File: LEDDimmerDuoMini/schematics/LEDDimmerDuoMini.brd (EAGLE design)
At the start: 82.2 x 22.9 mm, 13 parts, among them IC1 7805T, T1 2N3904, T2 2N3904

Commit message: Update before LED flaate testen
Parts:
- added R3, R4: (no value), eagle-ltspice:R0805
- moved Q2 5.68 mm to (33.0, 6.35), turned to 90 degrees
- moved C2 5.08 mm to (69.8, 14.0)
- moved C3 5.08 mm to (69.8, 9.53)
- moved IC1 5.08 mm to (64.8, 11.4)
- moved MINI_TWI 5.08 mm to (80.0, 12.1)
- moved TWI_PORT 5.08 mm to (84.5, 12.1)
- moved T2 4.62 mm to (40.6, 3.81), turned to 270 degrees
- moved R2 2.84 mm to (16.5, 6.35)
- moved JP1 2.54 mm to (59.7, 19.1)
- moved JP2 2.54 mm to (59.7, 3.81)
- moved Q1 2.54 mm to (33.0, 17.8), turned to 90 degrees
- moved T1 1.80 mm to (40.6, 15.2), turned to 270 degrees
- moved R1 1.80 mm to (16.5, 16.5)
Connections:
- new net N$7: Q2.G, R4.2, T2.3
- net PWM1: now also R3.1, R3.2
- net PWM2: now also R4.1; no longer Q2.G, T2.3
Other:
- board size 82.2 x 22.9 mm -> 87.3 x 22.9 mm

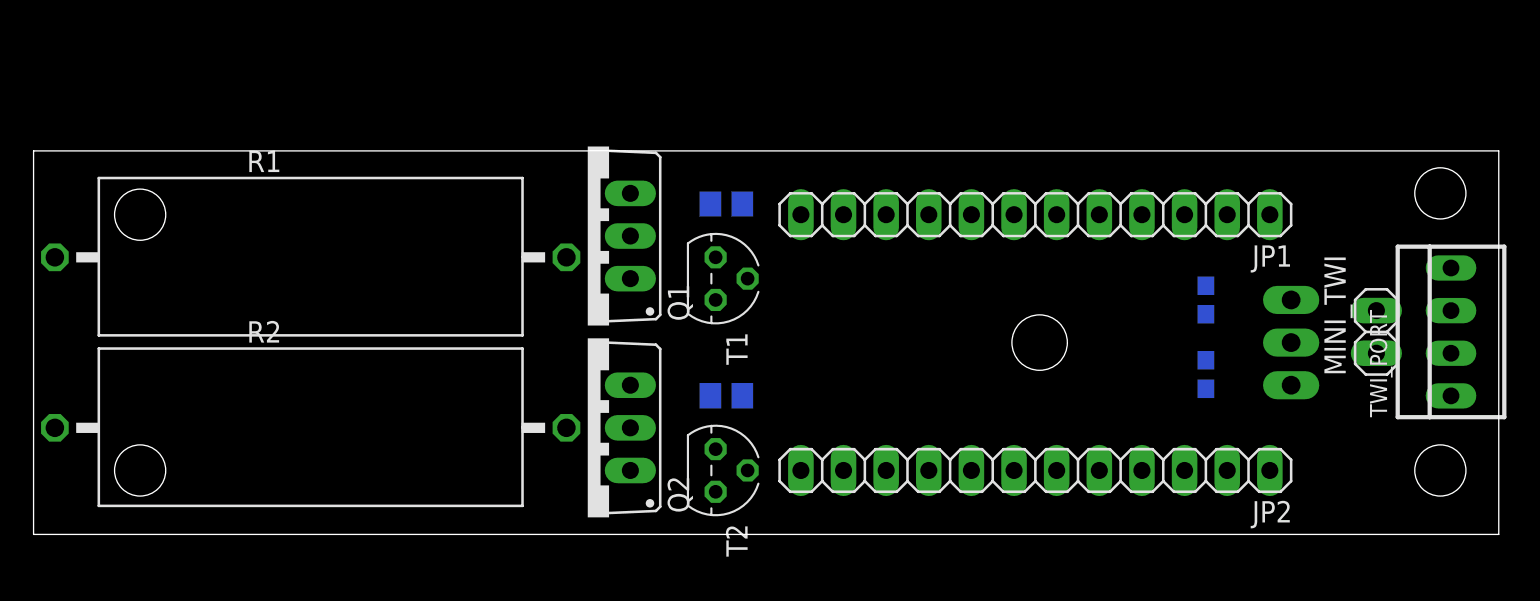
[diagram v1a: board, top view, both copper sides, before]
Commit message: Finished laying out components for LEEDDimmerDuoM<ini
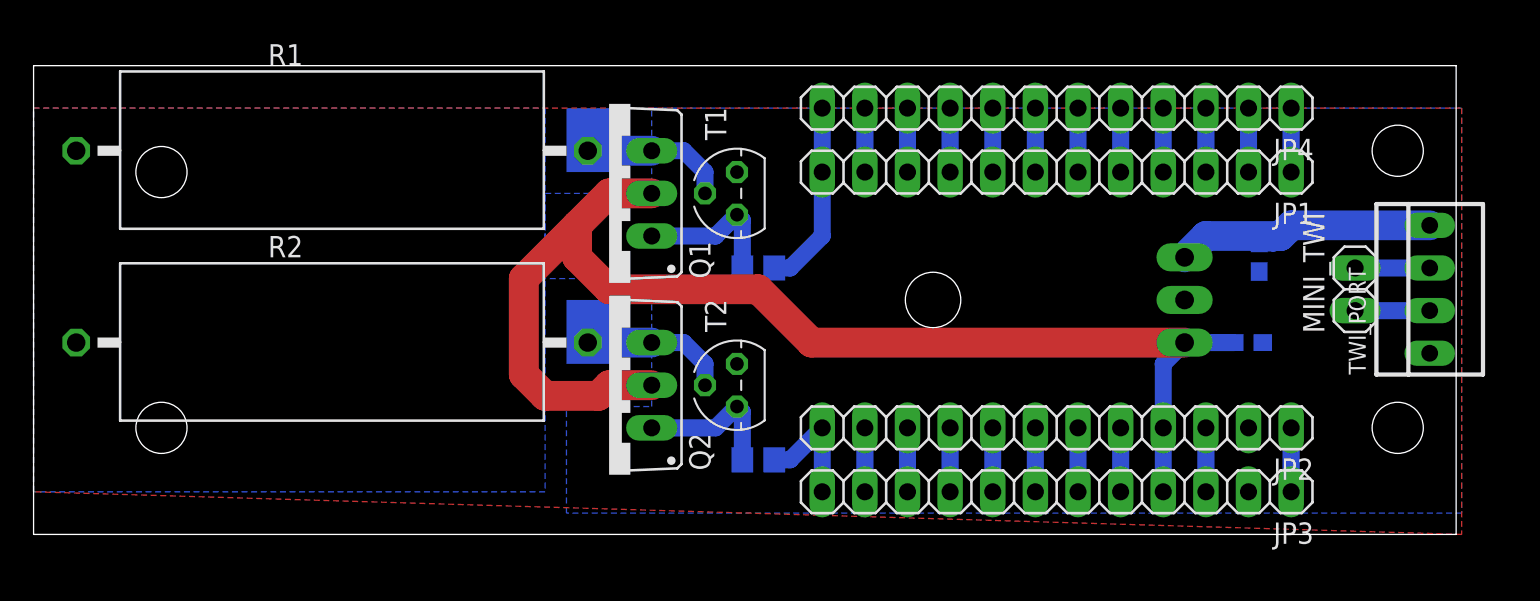
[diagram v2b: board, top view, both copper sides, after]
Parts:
- added JP3, JP4: (no value), pinhead:1X12
- moved IC1 6.84 mm to (58.4, 14.0)
- moved R1 6.48 mm to (17.8, 22.9)
- moved R2 5.24 mm to (17.8, 11.4)
- moved T1 5.24 mm to (41.9, 20.3), turned to 90 degrees
- moved T2 5.24 mm to (41.9, 8.89), turned to 90 degrees
- moved R4 4.26 mm to (43.2, 4.45)
- moved R3 4.26 mm to (43.2, 15.9)
- moved C2 4.07 mm to (73.0, 16.5)
- moved C3 3.18 mm to (72.4, 11.4), turned to 180 degrees
- moved MINI_TWI 2.84 mm to (78.7, 14.6)
- moved JP2 2.84 mm to (61.0, 6.35)
- moved JP1 2.84 mm to (61.0, 21.6)
- moved Q2 2.84 mm to (34.3, 8.89)
- moved TWI_PORT 2.84 mm to (83.2, 14.6)
- moved Q1 2.84 mm to (34.3, 20.3)
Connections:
- new net N$12: JP1.6, JP4.6
- new net N$13: JP1.9, JP4.9
- new net N$15: JP2.1, JP3.1
- new net N$17: JP2.3, JP3.3
- new net N$19: JP2.5, JP3.5
- new net N$20: JP2.6, JP3.6
- new net N$21: JP2.7, JP3.7
- new net N$22: JP2.8, JP3.8
- new net N$23: JP2.9, JP3.9
- new net N$24: JP2.10, JP3.10
- new net N$25: JP2.11, JP3.11
- new net N$6: JP1.3, JP4.3
- new net N$8: JP1.4, JP4.4
- new net N$9: JP1.5, JP4.5
- net 5V: now also JP3.4
- net GND: now also JP3.2
- net INA: now also JP4.8
- net INB: now also JP4.7
- net N$10: now also JP4.11
- net N$11: now also JP4.10
- net PWM1: now also JP4.12
- net PWM2: now also JP3.12
- net RX: now also JP4.2
- net TX: now also JP4.1
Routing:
- net 5V: track 0.00 -> 76.4 mm
- net PWM1: track 0.00 -> 20.2 mm
- net +12V: track 0.00 -> 17.3 mm
- net N$7: track 0.00 -> 8.91 mm
- net N$5: track 0.00 -> 8.78 mm
- net N$4: track 0.00 -> 8.78 mm
- net PWM2: track 0.00 -> 7.46 mm
- net N$3: track 0.00 -> 4.45 mm
- net N$2: track 0.00 -> 4.45 mm
- net N$25: track 0.00 -> 3.81 mm
- net N$24: track 0.00 -> 3.81 mm
- net N$23: track 0.00 -> 3.81 mm
- net N$22: track 0.00 -> 3.81 mm
- net N$21: track 0.00 -> 3.81 mm
- net N$20: track 0.00 -> 3.81 mm
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- added copper zone on layer 1, net GND
- added copper zone on layer 16, net GND
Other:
- board size 87.3 x 22.9 mm -> 84.8 x 27.9 mm
